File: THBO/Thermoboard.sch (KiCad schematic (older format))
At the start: 88 parts, among them J101 CONN_02X02, J102 CONN_02X02, J103 CONN_02X02, J104 CONN_02X02, J105 CONN_02X02, J106 CONN_02X02, J107 CONN_02X02, J108 CONN_02X02, J109 CONN_02X02, J110 CONN_02X02, J111 CONN_02X02, J112 CONN_02X02, J113 CONN_02X02, J114 CONN_02X02, J115 CONN_02X02, J116 CONN_02X02, J117 CONN_02X02, J118 CONN_02X02, J119 CONN_02X02, J120 CONN_02X02, J121 CONN_02X02, J122 CONN_02X02, J123 CONN_02X02, J124 CONN_02X02, J125 CONN_02X02, J126 CONN_02X02, J127 CONN_02X02, J128 CONN_02X02, J129 CONN_02X02, J130 CONN_02X02, J131 CONN_02X02, J132 CONN_02X02, J133 MOUNTING_HOLE, J134 MOUNTING_HOLE, J135 MOUNTING_HOLE, J136 MOUNTING_HOLE, P101 CONN_01X02, P102 CONN_02X08, P103 CONN_01X02, P104 CONN_02X08, P105 CONN_01X02, P106 CONN_01X02, P107 CONN_01X02, P108 CONN_01X02, P109 CONN_01X02, P110 CONN_01X02, P111 CONN_01X02, P112 CONN_01X02, P113 CONN_01X02, P114 CONN_01X02, P115 CONN_01X02, P116 CONN_01X02, P117 CONN_01X02, P118 CONN_01X02, P119 CONN_01X02, P120 CONN_01X02, P121 CONN_01X02, P122 CONN_01X02, P123 CONN_01X02, P124 CONN_01X02, P125 CONN_01X02, P126 CONN_01X02, P127 CONN_01X02, P128 CONN_01X02, P129 CONN_01X02, P130 CONN_01X02, P131 CONN_01X02, P132 CONN_01X02, P133 CONN_01X02, P134 CONN_01X02, P135 CONN_01X02, P136 CONN_01X02, U101 OPA380, U102 OPA380

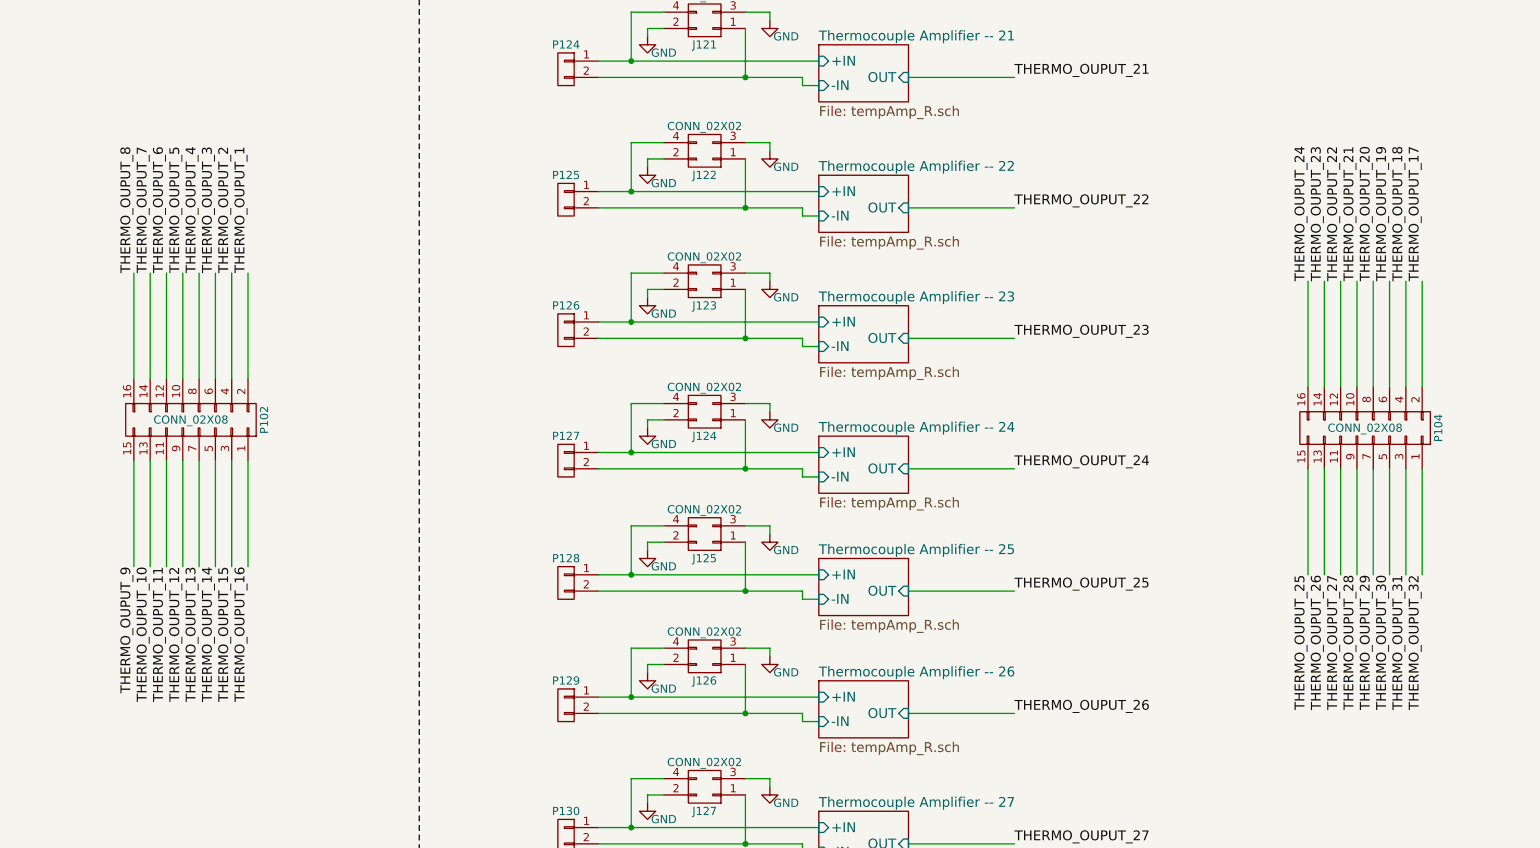
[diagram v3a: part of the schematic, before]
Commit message: Updated 16 Pin Connectors on THBO
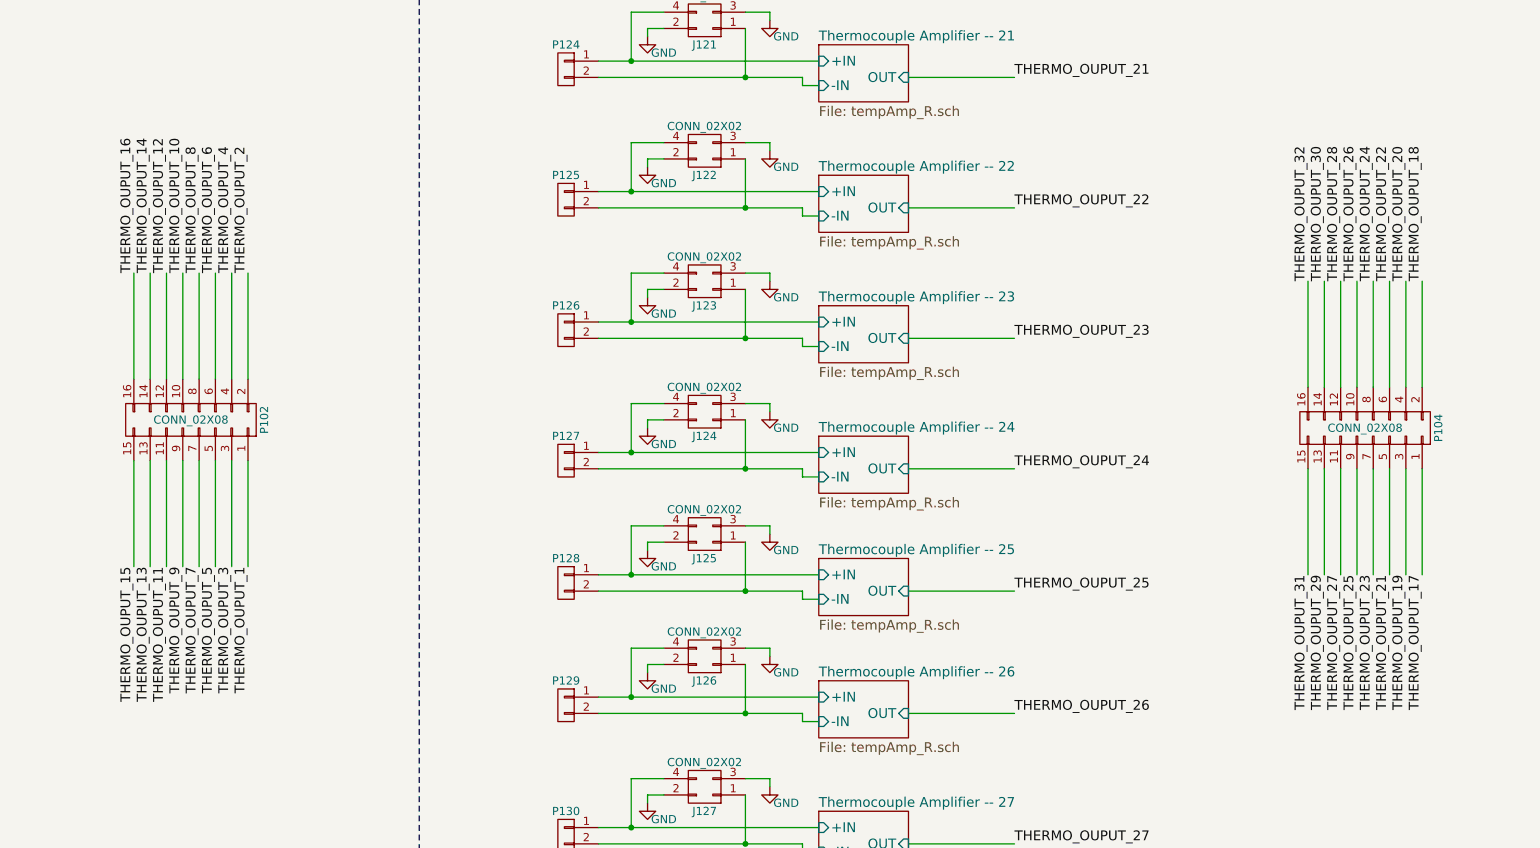
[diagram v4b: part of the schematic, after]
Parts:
- P102, P104: footprint moboFootprints:Molex_16pin_milliGrid -> moboFootprints:302-S161; Digikey P/N WM18864-ND -> ED10523-ND; Mfg. (none) -> On Shore Technology Inc.; Mfg. P/N (none) -> 302-S161
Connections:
- net THERMO_OUPUT_1: now also P102.1 (P1); no longer P102.2 (P2)
- net THERMO_OUPUT_10: now also P102.10 (P10); no longer P102.13 (P13)
- net THERMO_OUPUT_12: now also P102.12 (P12); no longer P102.9 (P9)
- net THERMO_OUPUT_13: now also P102.13 (P13); no longer P102.7 (P7)
- net THERMO_OUPUT_14: now also P102.14 (P14); no longer P102.5 (P5)
- net THERMO_OUPUT_15: now also P102.15 (P15); no longer P102.3 (P3)
- net THERMO_OUPUT_16: now also P102.16 (P16); no longer P102.1 (P1)
- net THERMO_OUPUT_17: now also P104.1 (P1); no longer P104.2 (P2)
- net THERMO_OUPUT_18: now also P104.2 (P2); no longer P104.4 (P4)
- net THERMO_OUPUT_19: now also P104.3 (P3); no longer P104.6 (P6)
- net THERMO_OUPUT_2: now also P102.2 (P2); no longer P102.4 (P4)
- net THERMO_OUPUT_20: now also P104.4 (P4); no longer P104.8 (P8)
- net THERMO_OUPUT_21: now also P104.5 (P5); no longer P104.10 (P10)
- net THERMO_OUPUT_22: now also P104.6 (P6); no longer P104.12 (P12)
- net THERMO_OUPUT_23: now also P104.7 (P7); no longer P104.14 (P14)
- net THERMO_OUPUT_24: now also P104.8 (P8); no longer P104.16 (P16)
- net THERMO_OUPUT_25: now also P104.9 (P9); no longer P104.15 (P15)
- net THERMO_OUPUT_26: now also P104.10 (P10); no longer P104.13 (P13)
- net THERMO_OUPUT_28: now also P104.12 (P12); no longer P104.9 (P9)
- net THERMO_OUPUT_29: now also P104.13 (P13); no longer P104.7 (P7)
- net THERMO_OUPUT_3: now also P102.3 (P3); no longer P102.6 (P6)
- net THERMO_OUPUT_30: now also P104.14 (P14); no longer P104.5 (P5)
- net THERMO_OUPUT_31: now also P104.15 (P15); no longer P104.3 (P3)
- net THERMO_OUPUT_32: now also P104.16 (P16); no longer P104.1 (P1)
- net THERMO_OUPUT_4: now also P102.4 (P4); no longer P102.8 (P8)
- net THERMO_OUPUT_5: now also P102.5 (P5); no longer P102.10 (P10)
- net THERMO_OUPUT_6: now also P102.6 (P6); no longer P102.12 (P12)
- net THERMO_OUPUT_7: now also P102.7 (P7); no longer P102.14 (P14)
- net THERMO_OUPUT_8: now also P102.8 (P8); no longer P102.16 (P16)
- net THERMO_OUPUT_9: now also P102.9 (P9); no longer P102.15 (P15)
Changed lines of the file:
@@
 F 0 "P102" H 6200 12300 50  0000 C CNN
 F 1 "CONN_02X08" V 6200 11850 50  0000 C CNN
-F 2 "moboFootprints:Molex_16pin_milliGrid" H 6200 10650 50  0001 C CNN
+F 2 "moboFootprints:302-S161" H 6200 10650 50  0001 C CNN
 F 3 "" H 6200 10650 50  0000 C CNN
-F 4 "WM18864-ND" H 6200 11850 60  0001 C CNN "Digikey P/N"
+F 4 "On Shore Technology Inc." H 6200 11850 60  0001 C CNN "Mfg."
+F 5 "302-S161" H 6200 11850 60  0001 C CNN "Mfg. P/N"
+F 6 "ED10523-ND" H 6200 11850 60  0001 C CNN "Digikey P/N"
 	1    6200 11850
 	0    1    -1   0
@@
 Wire Wire Line
 	5850 11600 5850 10950
-Text Label 5850 10950 1    60   ~ 0
+Text Label 6250 10950 1    60   ~ 0
 THERMO_OUPUT_8
 Wire Wire Line
 	5950 11600 5950 10950
-Text Label 5950 10950 1    60   ~ 0
+Text Label 6250 12750 3    60   ~ 0
 THERMO_OUPUT_7
 Wire Wire Line
 	6050 11600 6050 10950
-Text Label 6050 10950 1    60   ~ 0
+Text Label 6350 10950 1    60   ~ 0
 THERMO_OUPUT_6
 Wire Wire Line
 	6150 11600 6150 10950
+Text Label 6350 12750 3    60   ~ 0
+THERMO_OUPUT_5
+Wire Wire Line
+	6250 11600 6250 10950
+Text Label 6450 10950 1    60   ~ 0
+THERMO_OUPUT_4
+Wire Wire Line
+	6350 11600 6350 10950
+Text Label 6450 12750 3    60   ~ 0
+THERMO_OUPUT_3
+Wire Wire Line
+	6450 11600 6450 10950
+Text Label 6550 10950 1    60   ~ 0
+THERMO_OUPUT_2
+Wire Wire Line
+	6550 11600 6550 10950
+Text Label 6550 12750 3    60   ~ 0
+THERMO_OUPUT_1
+Wire Wire Line
+	5850 12100 5850 12750
+Text Label 6150 12750 3    60   ~ 0
+THERMO_OUPUT_9
+Wire Wire Line
+	5950 12100 5950 12750
 Text Label 6150 10950 1    60   ~ 0
-THERMO_OUPUT_5
-Wire Wire Line
-	6250 11600 6250 10950
-Text Label 6250 10950 1    60   ~ 0
-THERMO_OUPUT_4
-Wire Wire Line
-	6350 11600 6350 10950
-Text Label 6350 10950 1    60   ~ 0
-THERMO_OUPUT_3
-Wire Wire Line
-	6450 11600 6450 10950
-Text Label 6450 10950 1    60   ~ 0
-THERMO_OUPUT_2
-Wire Wire Line
-	6550 11600 6550 10950
-Text Label 6550 10950 1    60   ~ 0
-THERMO_OUPUT_1
-Wire Wire Line
-	5850 12100 5850 12750
-Text Label 5850 12750 3    60   ~ 0
-THERMO_OUPUT_9
-Wire Wire Line
-	5950 12100 5950 12750
-Text Label 5950 12750 3    60   ~ 0
 THERMO_OUPUT_10
 Wire Wire Line
@@
 Wire Wire Line
 	6150 12100 6150 12750
-Text Label 6150 12750 3    60   ~ 0
+Text Label 6050 10950 1    60   ~ 0
 THERMO_OUPUT_12
 Wire Wire Line
 	6250 12100 6250 12750
-Text Label 6250 12750 3    60   ~ 0
+Text Label 5950 12750 3    60   ~ 0
 THERMO_OUPUT_13
 Wire Wire Line
 	6350 12100 6350 12750
-Text Label 6350 12750 3    60   ~ 0
+Text Label 5950 10950 1    60   ~ 0
 THERMO_OUPUT_14
 Wire Wire Line
 	6450 12100 6450 12750
-Text Label 6450 12750 3    60   ~ 0
+Text Label 5850 12750 3    60   ~ 0
 THERMO_OUPUT_15
 Wire Wire Line
 	6550 12100 6550 12750
-Text Label 6550 12750 3    60   ~ 0
+Text Label 5850 10950 1    60   ~ 0
 THERMO_OUPUT_16
 $Comp
@@
 F 0 "P104" H 13400 12350 50  0000 C CNN
 F 1 "CONN_02X08" V 13400 11900 50  0000 C CNN
-F 2 "moboFootprints:Molex_16pin_milliGrid" H 13400 10700 50  0001 C CNN
+F 2 "moboFootprints:302-S161" H 13400 10700 50  0001 C CNN
 F 3 "" H 13400 10700 50  0000 C CNN
-F 4 "WM18864-ND" H 13400 11900 60  0001 C CNN "Digikey P/N"
+F 4 "On Shore Technology Inc." H 13400 11900 60  0001 C CNN "Mfg."
+F 5 "302-S161" H 13400 11900 60  0001 C CNN "Mfg. P/N"
+F 6 "ED10523-ND" H 13400 11900 60  0001 C CNN "Digikey P/N"
 	1    13400 11900
 	0    1    -1   0
@@
 Wire Wire Line
 	13050 11650 13050 11000
+Text Label 13450 11000 1    60   ~ 0
+THERMO_OUPUT_24
+Wire Wire Line
+	13150 11650 13150 11000
+Text Label 13450 12800 3    60   ~ 0
+THERMO_OUPUT_23
+Wire Wire Line
+	13250 11650 13250 11000
+Text Label 13550 11000 1    60   ~ 0
+THERMO_OUPUT_22
+Wire Wire Line
+	13350 11650 13350 11000
+Text Label 13550 12800 3    60   ~ 0
+THERMO_OUPUT_21
+Wire Wire Line
+	13450 11650 13450 11000
+Text Label 13650 11000 1    60   ~ 0
+THERMO_OUPUT_20
+Wire Wire Line
+	13550 11650 13550 11000
+Text Label 13650 12800 3    60   ~ 0
+THERMO_OUPUT_19
+Wire Wire Line
+	13650 11650 13650 11000
+Text Label 13750 11000 1    60   ~ 0
+THERMO_OUPUT_18
+Wire Wire Line
+	13750 11650 13750 11000
+Text Label 13750 12800 3    60   ~ 0
+THERMO_OUPUT_17
+Wire Wire Line
+	13050 12150 13050 12800
 Text Label 13050 11000 1    60   ~ 0
-THERMO_OUPUT_24
-Wire Wire Line
-	13150 11650 13150 11000
+THERMO_OUPUT_32
+Wire Wire Line
+	13150 12150 13150 12800
+Text Label 13050 12800 3    60   ~ 0
+THERMO_OUPUT_31
+Wire Wire Line
+	13250 12150 13250 12800
 Text Label 13150 11000 1    60   ~ 0
-THERMO_OUPUT_23
-Wire Wire Line
-	13250 11650 13250 11000
+THERMO_OUPUT_30
+Wire Wire Line
+	13350 12150 13350 12800
+Text Label 13150 12800 3    60   ~ 0
+THERMO_OUPUT_29
+Wire Wire Line
+	13450 12150 13450 12800
 Text Label 13250 11000 1    60   ~ 0
-THERMO_OUPUT_22
-Wire Wire Line
-	13350 11650 13350 11000
-Text Label 13350 11000 1    60   ~ 0
-THERMO_OUPUT_21
-Wire Wire Line
-	13450 11650 13450 11000
-Text Label 13450 11000 1    60   ~ 0
-THERMO_OUPUT_20
-Wire Wire Line
-	13550 11650 13550 11000
-Text Label 13550 11000 1    60   ~ 0
-THERMO_OUPUT_19
-Wire Wire Line
-	13650 11650 13650 11000
-Text Label 13650 11000 1    60   ~ 0
-THERMO_OUPUT_18
-Wire Wire Line
-	13750 11650 13750 11000
-Text Label 13750 11000 1    60   ~ 0
-THERMO_OUPUT_17
-Wire Wire Line
-	13050 12150 13050 12800
-Text Label 13750 12800 3    60   ~ 0
-THERMO_OUPUT_32
-Wire Wire Line
-	13150 12150 13150 12800
-Text Label 13650 12800 3    60   ~ 0
-THERMO_OUPUT_31
-Wire Wire Line
-	13250 12150 13250 12800
-Text Label 13550 12800 3    60   ~ 0
-THERMO_OUPUT_30
-Wire Wire Line
-	13350 12150 13350 12800
-Text Label 13450 12800 3    60   ~ 0
-THERMO_OUPUT_29
-Wire Wire Line
-	13450 12150 13450 12800
-Text Label 13350 12800 3    60   ~ 0
 THERMO_OUPUT_28
 Wire Wire Line
@@
 Wire Wire Line
 	13650 12150 13650 12800
-Text Label 13150 12800 3    60   ~ 0
+Text Label 13350 11000 1    60   ~ 0
 THERMO_OUPUT_26
 Wire Wire Line
 	13750 12150 13750 12800
-Text Label 13050 12800 3    60   ~ 0
+Text Label 13350 12800 3    60   ~ 0
 THERMO_OUPUT_25
 Wire Wire Line
